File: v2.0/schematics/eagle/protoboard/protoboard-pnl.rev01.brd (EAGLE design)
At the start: 30 x 128 mm, 0 parts

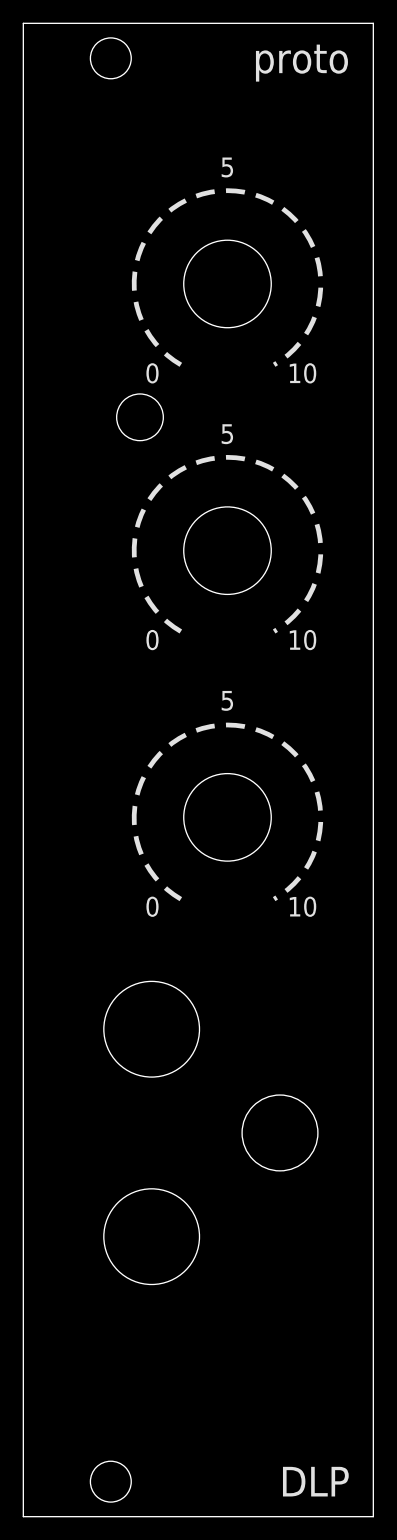
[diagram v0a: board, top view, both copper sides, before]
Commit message: Panel revisions; VCF-LP board layout
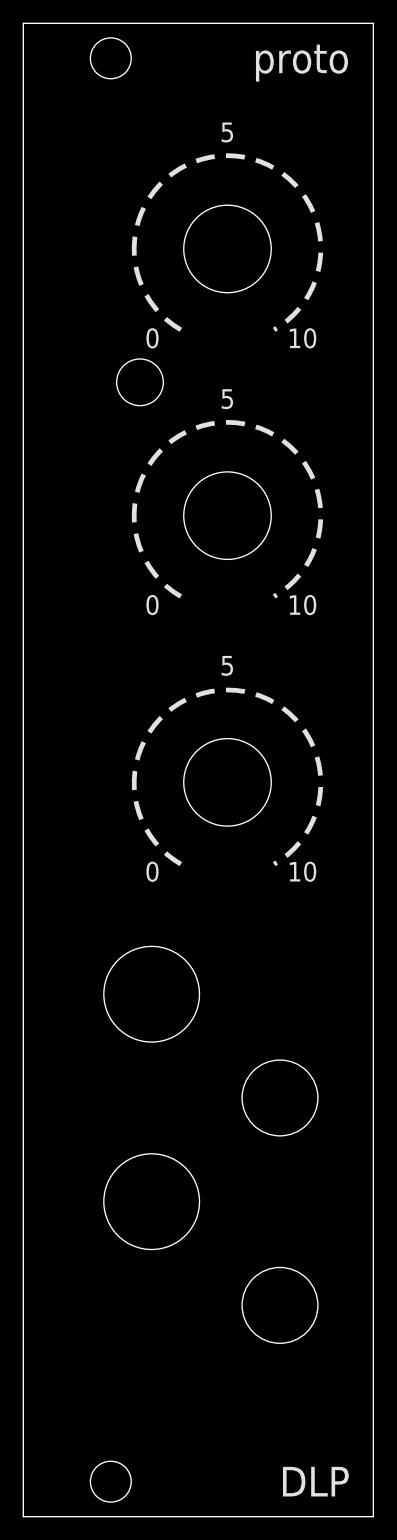
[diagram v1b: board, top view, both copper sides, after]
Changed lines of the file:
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@@
 <wire x1="30" y1="128" x2="0" y2="128" width="0" layer="20"/>
 <wire x1="0" y1="128" x2="0" y2="0" width="0" layer="20"/>
-<hole x="17.5" y="82.8" drill="7.5" grouprefs="POTS"/>
-<hole x="11" y="41.78" drill="8.2" grouprefs="JACKS"/>
-<hole x="11" y="24" drill="8.2" grouprefs="JACKS"/>
-<hole x="17.5" y="59.94" drill="7.5" grouprefs="POTS"/>
-<hole x="17.5" y="105.66" drill="7.5" grouprefs="POTS"/>
-<hole x="22" y="32.89" drill="6.5"/>
-<hole x="10" y="94.23" drill="4"/>
+<hole x="17.5" y="85.8" drill="7.5" grouprefs="POTS"/>
+<hole x="11" y="44.78" drill="8.2" grouprefs="JACKS"/>
+<hole x="11" y="27" drill="8.2" grouprefs="JACKS"/>
+<hole x="17.5" y="62.94" drill="7.5" grouprefs="POTS"/>
+<hole x="17.5" y="108.66" drill="7.5" grouprefs="POTS"/>
+<hole x="22" y="35.89" drill="6.5"/>
+<hole x="10" y="97.23" drill="4"/>
 <hole x="7.5" y="125" drill="3.5"/>
 <hole x="7.5" y="3" drill="3.5"/>
 <text x="28" y="3" size="2.54" layer="25" align="center-right">DLP</text>
 <text x="28" y="125" size="2.54" layer="25" align="center-right">proto</text>
-<wire x1="13.5" y1="98.73" x2="21.5" y2="98.73" width="0.4064" layer="25" style="shortdash" curve="-300"/>
-<wire x1="13.5" y1="75.87" x2="21.5" y2="75.87" width="0.4064" layer="25" style="shortdash" curve="-300"/>
-<wire x1="13.5" y1="52.93" x2="21.5" y2="52.93" width="0.4064" layer="25" style="shortdash" curve="-300"/>
-<text x="11.072" y="98" size="1.6764" layer="25" align="center">0</text>
-<text x="23.928" y="98" size="1.6764" layer="25" align="center">10</text>
-<text x="17.5" y="115.66" size="1.6764" layer="25" align="center">5</text>
-<text x="11.072" y="75.14" size="1.6764" layer="25" align="center">0</text>
-<text x="17.5" y="92.8" size="1.6764" layer="25" align="center">5</text>
-<text x="23.928" y="75.14" size="1.6764" layer="25" align="center">10</text>
-<text x="23.928" y="52.28" size="1.6764" layer="25" align="center">10</text>
-<text x="17.5" y="69.94" size="1.6764" layer="25" align="center">5</text>
-<text x="11.072" y="52.28" size="1.6764" layer="25" align="center">0</text>
+<wire x1="13.5" y1="101.73" x2="21.5" y2="101.73" width="0.4064" layer="25" style="shortdash" curve="-300"/>
+<wire x1="13.5" y1="78.87" x2="21.5" y2="78.87" width="0.4064" layer="25" style="shortdash" curve="-300"/>
+<wire x1="13.5" y1="55.93" x2="21.5" y2="55.93" width="0.4064" layer="25" style="shortdash" curve="-300"/>
+<text x="11.072" y="101" size="1.6764" layer="25" align="center">0</text>
+<text x="23.928" y="101" size="1.6764" layer="25" align="center">10</text>
+<text x="17.5" y="118.66" size="1.6764" layer="25" align="center">5</text>
+<text x="11.072" y="78.14" size="1.6764" layer="25" align="center">0</text>
+<text x="17.5" y="95.8" size="1.6764" layer="25" align="center">5</text>
+<text x="23.928" y="78.14" size="1.6764" layer="25" align="center">10</text>
+<text x="23.928" y="55.28" size="1.6764" layer="25" align="center">10</text>
+<text x="17.5" y="72.94" size="1.6764" layer="25" align="center">5</text>
+<text x="11.072" y="55.28" size="1.6764" layer="25" align="center">0</text>
+<hole x="22" y="18.11" drill="6.5"/>
 </plain>
 <attributes>
